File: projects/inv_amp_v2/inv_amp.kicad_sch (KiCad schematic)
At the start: 5 parts, among them U1 NE5532

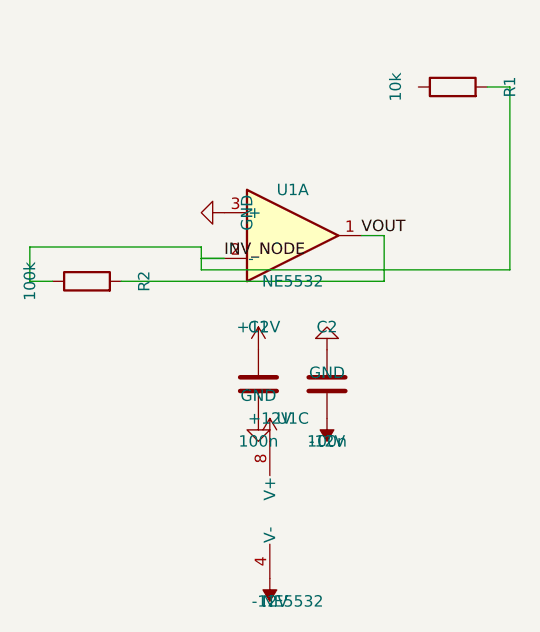
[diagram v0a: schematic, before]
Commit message: Phase 0: KiCad 10 migration + fix blind ERC parsing
- kicad-cli writes JSON reports only to -o file, never stdout; runner
  now uses a temp report file and real JSON decoding
- DetectKicadCLI exported and reused by render_sch and export_test
- KiCad 10 symbol renames (ATmega328-AU -> ATmega328-A) and pin
  numbers fixed in demos

Co-Authored-By: Claude Fable 5 <noreply@anthropic.com>
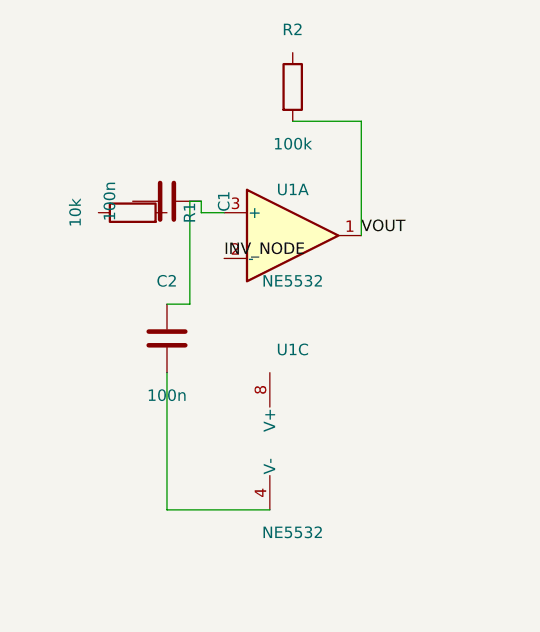
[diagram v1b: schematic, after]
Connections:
- net INV_NODE: no longer R1.2, R2.1
- net +12V: no longer names the net of U1.8 (V+)
- net +12V: no longer C1.1
- net -12V: no longer names the net of C2.2, U1.4 (V-)
- net GND: no longer names the net of C1.2, C2.1, U1.3 (+)
